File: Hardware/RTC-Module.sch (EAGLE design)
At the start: 23 parts, among them J4 455-1750-1-ND

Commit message: updated sensor
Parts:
- removed R4: 4.7k, SparkFun-Resistors:4.7KOHM1/10W1%(0603)
- removed RTC1: DS3231M, SparkFun-Clocks:DS3231M
- removed SJ1: (no value), SparkFun-Passives:SOLDERJUMPER_2WAYPASTE1&2&3
- added C2: 10nF, SparkFun-Capacitors:10NF-0603-50V-10%
- added D1: 0.5A/40V/420mV, SparkFun-DiscreteSemi:DIODE-SCHOTTKY-PMEG4005EJ
- added D2: 120mA/40V/370mV, SparkFun-DiscreteSemi:DIODE-SCHOTTKY-RB751S40
- added JP1: JUMPER-SMT_2_NC_PASTE_SILK, SparkFun-Jumpers:JUMPER-SMT_2_NC_PASTE_SILK
- added R5: 1k, SparkFun-Resistors:1KOHM-0603-1/10W-1%
- added U1: RV-4162-C7, SparkFun-Clocks:RV-4162-C7
- C1: value 0.1uF -> 1.0uF; device SparkFun-Capacitors:0.1UF-25V(+80/-20%)(0603) -> SparkFun-Capacitors:1.0UF-0603-16V-10%
- J3: device SparkFun-Connectors:CONN_04 -> SparkFun-Connectors:CONN_041X04_NO_SILK
- J4: value 455-1750-1-ND -> (none); device SparkFun-Connectors:CONN_03 -> SparkFun-Connectors:CONN_01PTH_NO_SILK_YES_STOP
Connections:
- removed net !INT/SQW: J4.2, R4.1, RTC1.SQW
- removed net !RST: J4.1, RTC1.RST
- removed net 32KHZ: J4.3, R3.1, RTC1.32KHZ
- removed net N$1: BAT1.+, RTC1.VBAT
- removed net N$3: R4.2, SJ1.1
- new net !INT: J4.1, R3.1, U1.!INT
- new net BATTERY: BAT1.+, C1.1, D2.A, R5.1
- new net CLKOUT: U1.CLKOUT
- new net N$4: D1.C, R5.2
- net 3.3V: now also C2.1, D1.A, D2.C, JP1.2, U1.VDD; no longer C1.1, RTC1.VCC, SJ1.2
- net GND: now also C2.2, U1.GND; no longer RTC1.GND
- net N$2: now also JP1.1; no longer SJ1.3
- net SCL: now also U1.SCL; no longer RTC1.SCL
- net SDA: now also U1.SDA; no longer RTC1.SDA
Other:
- note removed: "Address: 0xD0"
- note removed: "Clear jumper to disable I2C pullups"
- note removed: "Clear jumper to disable pullups for 32KHZ signal and the Interrupt/1HZ square wave"
- note removed: "Qwiic Headers"
- note removed: "RTC Module"
- moved on the sheet: BAT1, C1, J3, R1, R2, R3, SJ2

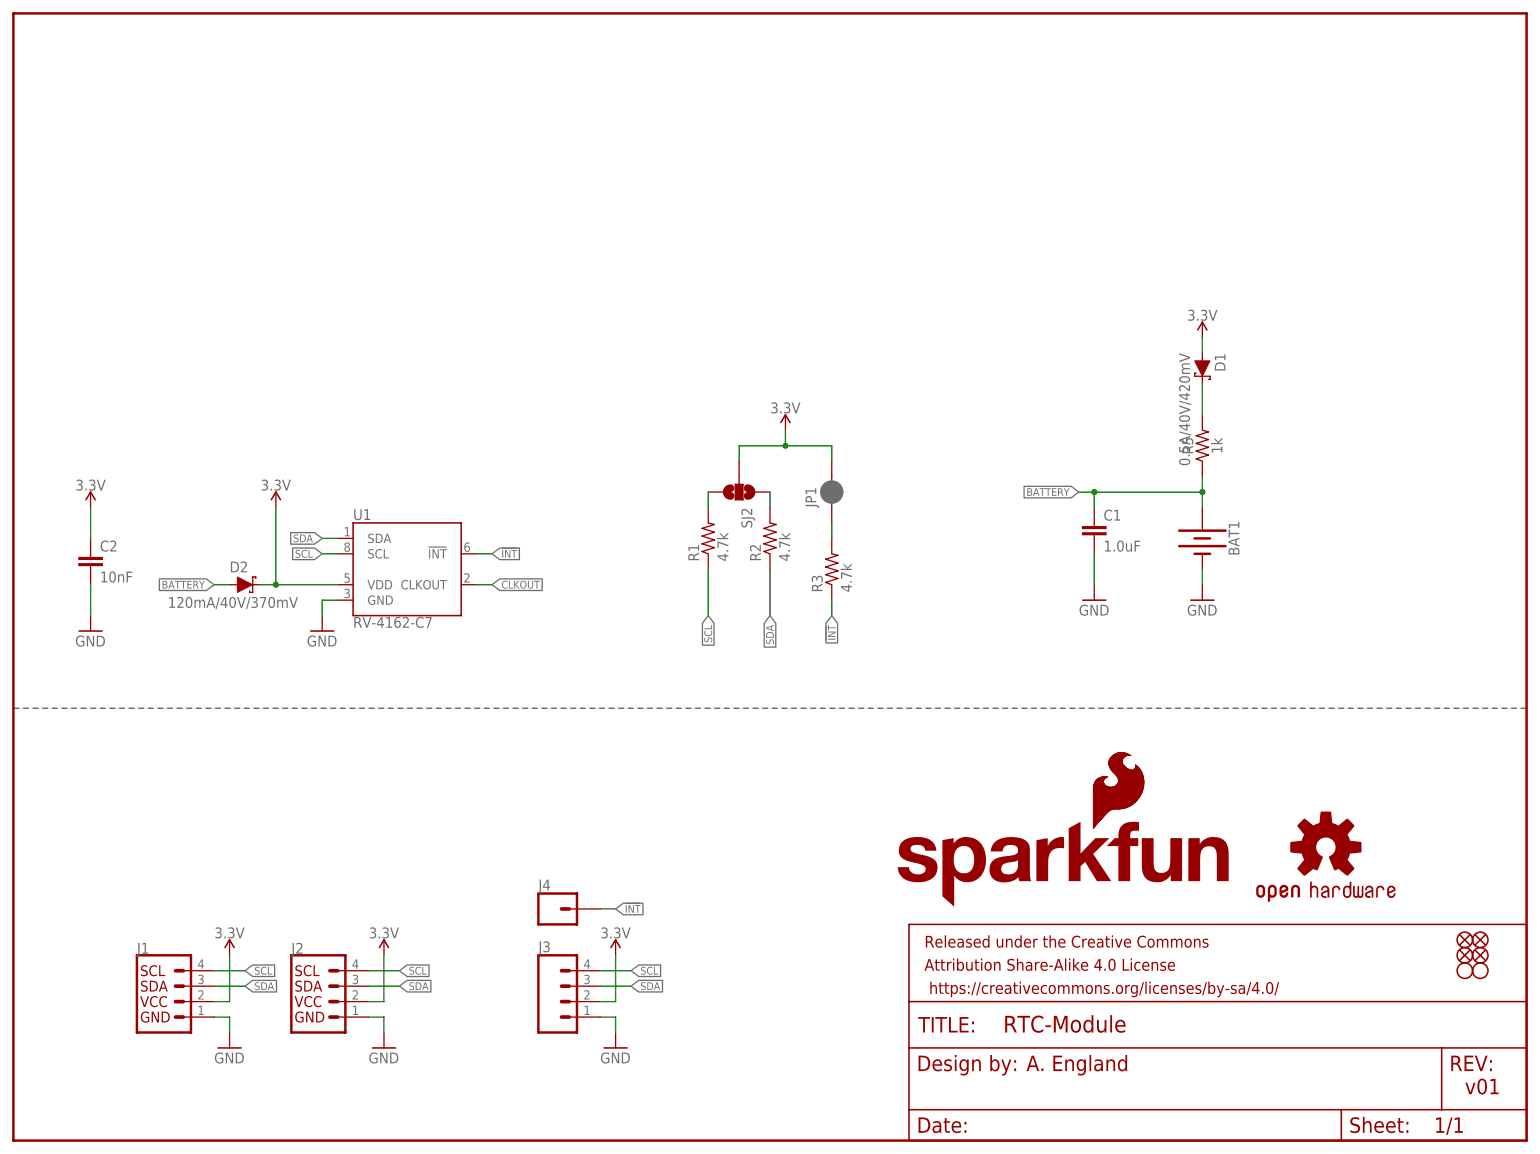
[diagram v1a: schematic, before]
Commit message: Updated RTC module
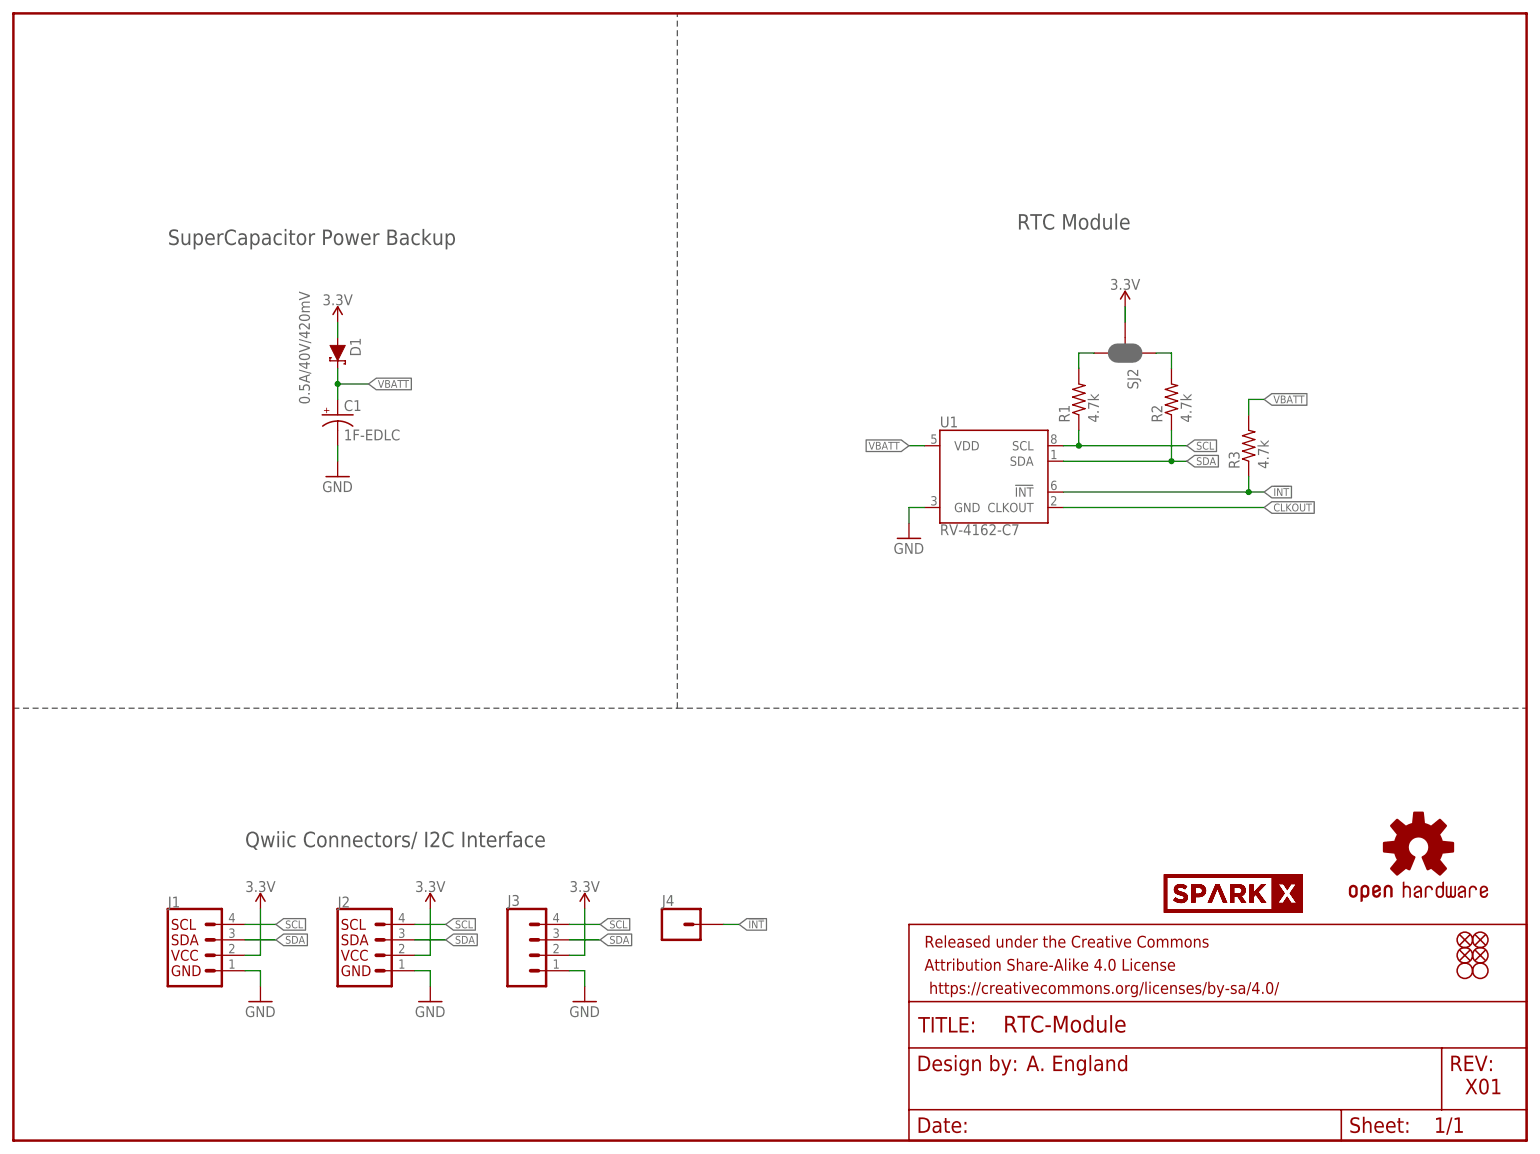
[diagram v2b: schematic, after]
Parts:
- removed BAT1: (no value), SparkFun-Batteries:BATTERY-12MM_PTH
- removed C2: 10nF, SparkFun-Capacitors:10NF-0603-50V-10%
- removed D2: 120mA/40V/370mV, SparkFun-DiscreteSemi:DIODE-SCHOTTKY-RB751S40
- removed JP1: JUMPER-SMT_2_NC_PASTE_SILK, SparkFun-Jumpers:JUMPER-SMT_2_NC_PASTE_SILK
- removed LOGO2: SFE_LOGO_FLAME.1_INCH, SparkFun-Aesthetics:SFE_LOGO_FLAME.1_INCH
- removed LOGO3: SFE_LOGO_NAME_FLAME.1_INCH, SparkFun-Aesthetics:SFE_LOGO_NAME_FLAME.1_INCH
- removed R5: 1k, SparkFun-Resistors:1KOHM-0603-1/10W-1%
- added U$3: SPARKX-LOGO2, SparkX:SPARKX-LOGO2
- added U$5: SPARKX-LOGO4, SparkX:SPARKX-LOGO4
- C1: value 1.0uF -> 1F-EDLC; device SparkFun-Capacitors:1.0UF-0603-16V-10% -> SparkFun-Capacitors:1F-EDLC
- SJ2: value (none) -> JUMPER-SMT_3_2-NC_PASTE_NO-SILK; device SparkFun-Passives:SOLDERJUMPER_2WAYPASTE1&2&3 -> SparkFun-Jumpers:JUMPER-SMT_3_2-NC_PASTE_NO-SILK
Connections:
- removed net BATTERY: BAT1.+, C1.1, D2.A, R5.1
- removed net N$2 (its old number): JP1.1, R3.2
- removed net N$4: D1.C, R5.2
- new net VBATT: C1.+, D1.C, R3.2, U1.VDD
- net 3.3V: no longer C2.1, D2.C, JP1.2, U1.VDD
- net GND: now also C1.-; no longer BAT1.-, C1.2, C2.2
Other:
- note added: "Qwiic Connectors/ I2C Interface"
- note added: "RTC Module"
- note added: "SuperCapacitor Power Backup"
- note added: "X01"
- note removed: "v01"
- moved on the sheet: D1, J1, J2, J3, J4, R1, R2, R3, U1

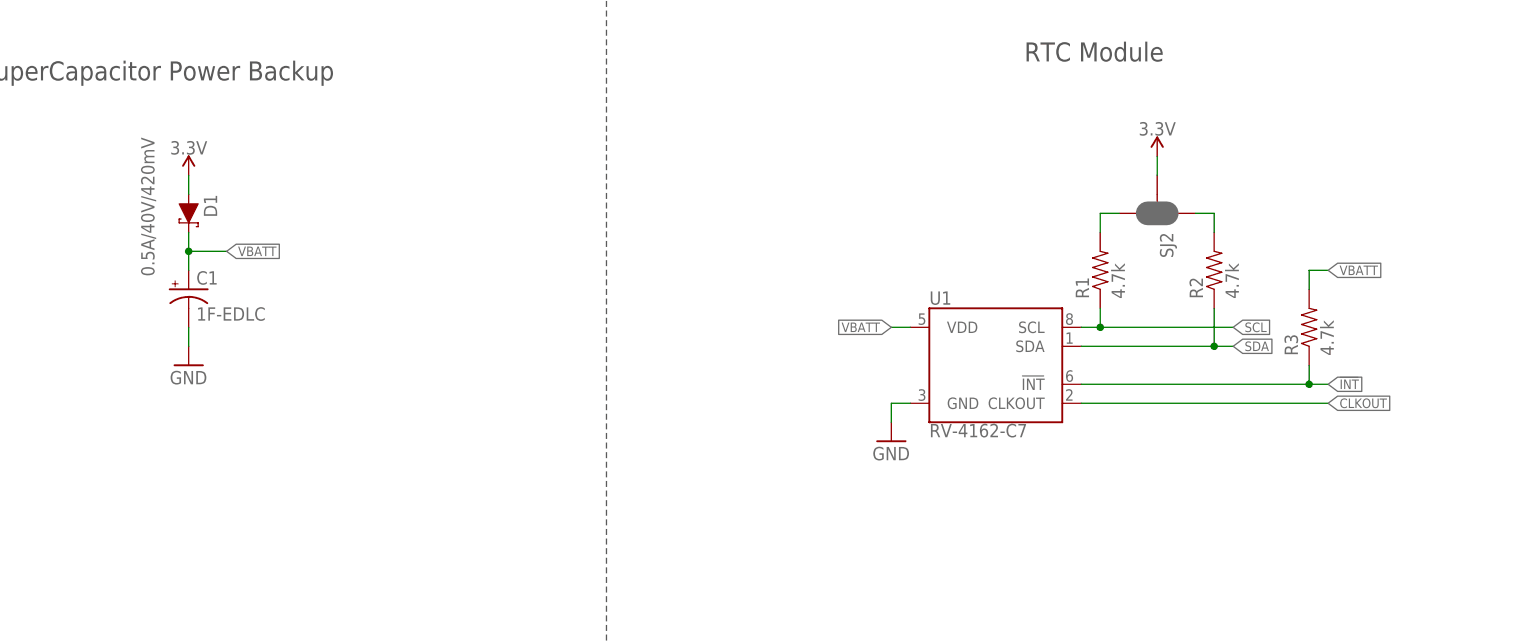
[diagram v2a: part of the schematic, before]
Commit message: updated to RV-1805
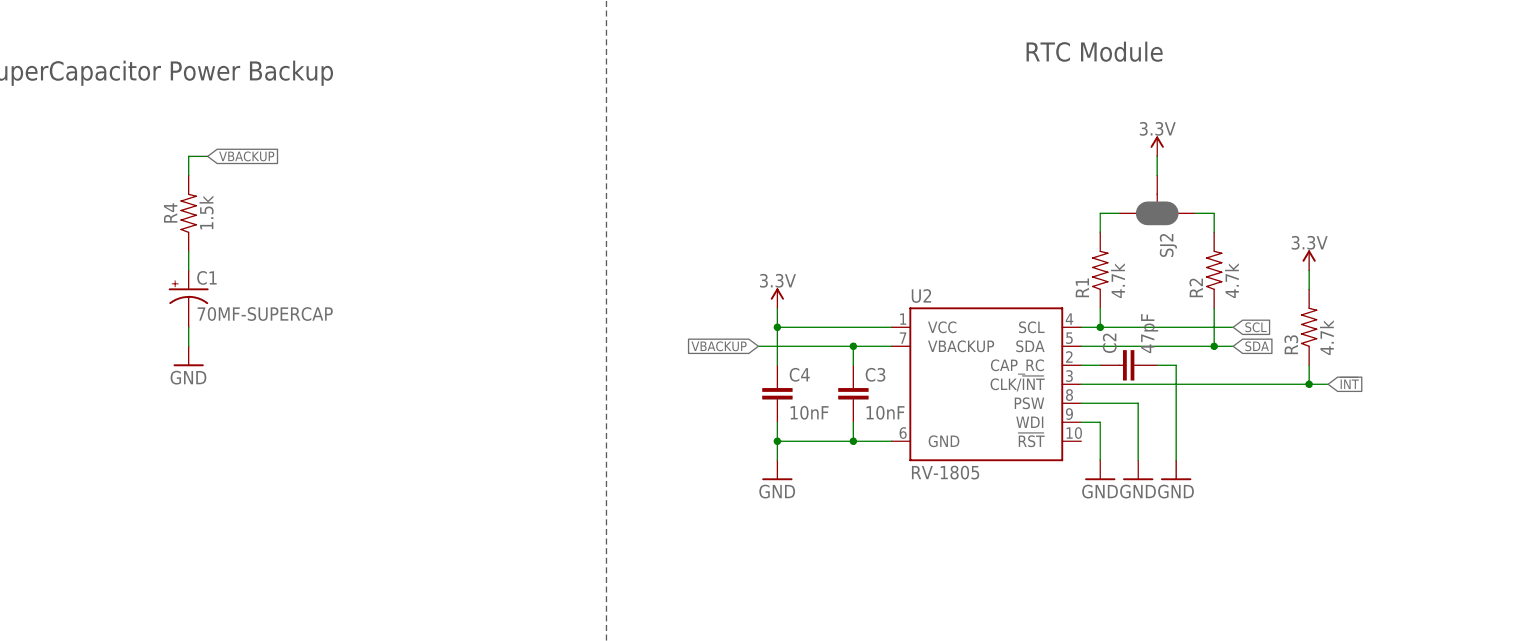
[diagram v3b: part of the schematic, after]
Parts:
- removed D1: 0.5A/40V/420mV, SparkFun-DiscreteSemi:DIODE-SCHOTTKY-PMEG4005EJ
- removed U1: RV-4162-C7, SparkFun-Clocks:RV-4162-C7
- added C2: 47pF, SparkFun-Capacitors:47PF-0603-50V-5%
- added C3, C4: 10nF, SparkFun-Capacitors:10NF-0603-50V-10%
- added R4: 1.5k, SparkFun-Resistors:1.5KOHM-0603-1/10W-1%
- added U2: RV-1805, SparkFun-Clocks:RV-1805
- C1: value 1F-EDLC -> 70MF-SUPERCAP; device SparkFun-Capacitors:1F-EDLC -> SparkFun-Capacitors:70MF-SUPERCAP
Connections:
- removed net CLKOUT: U1.CLKOUT
- removed net VBATT: C1.+, D1.C, R3.2, U1.VDD
- new net N$3: C1.+, R4.1
- new net N$4: C2.1, U2.CAP_RC
- new net VBACKUP: C3.1, R4.2, U2.VBACKUP
- net !INT: now also U2.CLK/!INT; no longer U1.!INT
- net 3.3V: now also C4.1, R3.2, U2.VCC; no longer D1.A
- net GND: now also C2.2, C3.2, C4.2, U2.GND, U2.PSW, U2.WDI; no longer U1.GND
- net SCL: now also U2.SCL; no longer U1.SCL
- net SDA: now also U2.SDA; no longer U1.SDA

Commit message: updated cap value
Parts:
- C1: value 70MF-SUPERCAP -> 220MF-SUPERCAP; device SparkFun-Capacitors:70MF-SUPERCAP -> SparkFun-Capacitors:220MF-SUPERCAP
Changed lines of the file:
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@@
 <part name="GND7" library="SparkFun" deviceset="GND" device=""/>
 <part name="SUPPLY4" library="SparkFun-PowerSymbols" deviceset="3.3V" device=""/>
-<part name="C1" library="SparkFun-Capacitors" deviceset="70MF-SUPERCAP" device=""/>
+<part name="C1" library="SparkFun-Capacitors" deviceset="220MF-SUPERCAP" device=""/>
 <part name="U$3" library="SparkX" deviceset="SPARKX-LOGO" device="2"/>
 <part name="U$5" library="SparkX" deviceset="SPARKX-LOGO" device="4"/>

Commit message: Updated cap footprint, broke out rest of pins
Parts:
- added R5, R6: 2.55k, SparkFun-Resistors:2.55KOHM-0603-1/10W-1%
- added R7: 4.7k, SparkFun-Resistors:4.7KOHM1/10W1%(0603)
- C1: value 220MF-SUPERCAP -> .22F-SUPERCAP; device SparkFun-Capacitors:220MF-SUPERCAP -> SparkFun-Capacitors:.22F-SUPERCAP
- J4: device SparkFun-Connectors:CONN_01PTH_NO_SILK_YES_STOP -> SparkFun-Connectors:CONN_031X03_NO_SILK
- R4: value 1.5k -> 4.7k; device SparkFun-Resistors:1.5KOHM-0603-1/10W-1% -> SparkFun-Resistors:4.7KOHM1/10W1%(0603)
- SJ2: value JUMPER-SMT_3_2-NC_PASTE_NO-SILK -> JUMPER-SMT_3_2-NC_PASTE_SILK; device SparkFun-Jumpers:JUMPER-SMT_3_2-NC_PASTE_NO-SILK -> SparkFun-Jumpers:JUMPER-SMT_3_2-NC_PASTE_SILK
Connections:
- removed net N$3: C1.+, R4.1
- new net !RST: J4.1, R4.1, U2.!RST
- new net N$5: C1.+, R5.1, R6.1
- new net PSW: J4.3, R7.1, U2.PSW
- net !INT: now also J4.2; no longer J4.1
- net 3.3V: now also R4.2, R7.2
- net GND: no longer U2.PSW
- net VBACKUP: now also R5.2, R6.2; no longer R4.2
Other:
- moved on the sheet: C1, C2, C3, C4, R1, R2, R4, SJ2, U2

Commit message: Changed pull ups, super cap silk, added panel.
Removed dupicate resistor on super cap. Removed pin 1 silk on super cap. Change I2C pull ups to 2.2k for 3.3V devices. Changed pull ups to 10k for lower draw. Added panel.
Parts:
- removed R5: 2.55k, SparkFun-Resistors:2.55KOHM-0603-1/10W-1%
- J1, J2: value (none) -> SMD
- J3: value (none) -> PTH
- R1, R2: value 4.7k -> 2.2k; device SparkFun-Resistors:4.7KOHM1/10W1%(0603) -> SparkFun-Resistors:2.2KOHM-0603-1/10W-1%
- R3, R4, R7: value 4.7k -> 10k; device SparkFun-Resistors:4.7KOHM1/10W1%(0603) -> SparkFun-Resistors:10KOHM-0603-1/10W-1%
- R6: value 2.55k -> 1K
- U$3: value SPARKX-LOGO2 -> SPARKX-LOGO4; device SparkX:SPARKX-LOGO2 -> SparkX:SPARKX-LOGO4
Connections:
- net N$5: no longer R5.1
- net VBACKUP: no longer R5.2
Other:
- moved on the sheet: C2, C3, C4, R6
